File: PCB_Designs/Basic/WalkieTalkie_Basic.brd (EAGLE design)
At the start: 27.9 x 27.9 mm, 35 parts, among them Q1 MOSFET-NCHANNELBSS123LT1G, U1 ATMEGA328P

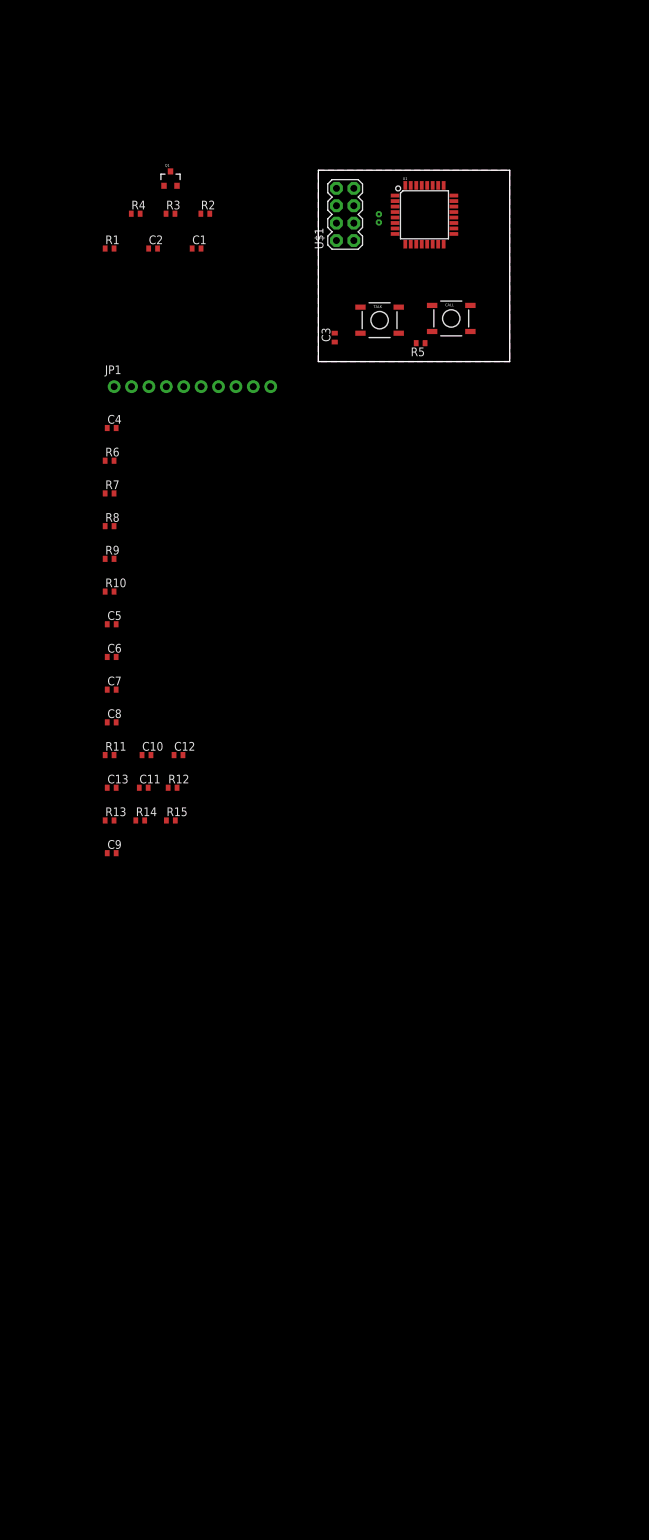
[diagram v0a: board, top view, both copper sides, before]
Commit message: updating pcb design with labels, removed extra button, added library part for nRF24L01 breakout, etc
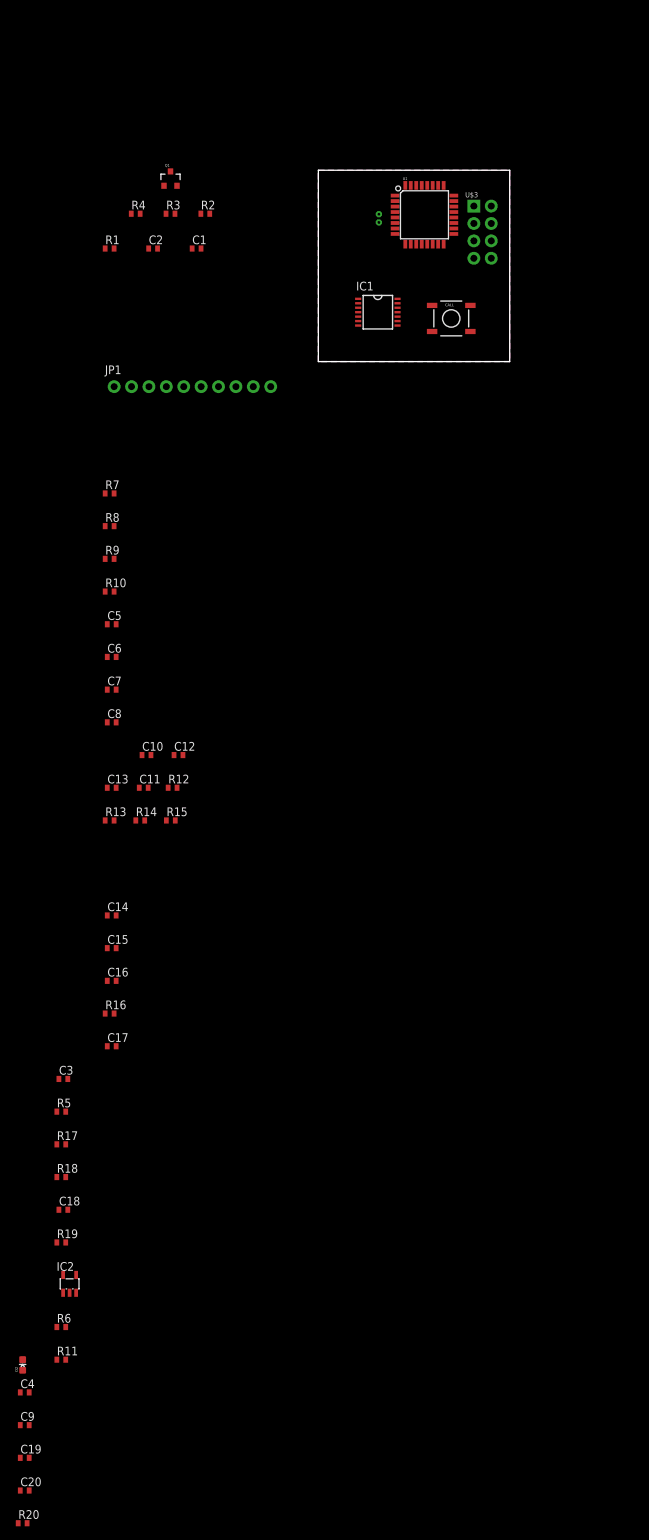
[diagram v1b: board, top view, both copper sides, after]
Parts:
- removed TALK: TAC_SWITCHSMD, SparkFun-Retired:TACTILE-SWITCH-SMD
- removed U$1: M04X2, SparkFun-Connectors:2X4
- added C14, C15, C16, C17, C19, C20: 100n, resistor:C0402
- added C18: 10n, resistor:C0402
- added D2: RED, SparkFun-LED:LED-0603
- added IC1: AD8609RU, analog-devices:TSSOP14
- added IC2: AD8603UJ, analog-devices:SOT23-5
- added R16: 10k, resistor:R0402
- added R17, R18, R19: 1.5k, resistor:R0402
- added R20: 1k, resistor:R0402
- added U$3: NRF24L01-BREAKOUT, Orlando:NRF24L01-BREAKOUT
- C3: value 100n -> 10n
- C4, C9: value 10n -> 100n
- R11, R6: value 1.5M -> 1.5k
- R5: value 10k -> 1.5M
- moved C4 141.4 mm to (-42.9, -150.5)
- moved R6 126.7 mm to (-37.5, -141.0)
- moved R5 123.9 mm to (-37.5, -109.5), turned to 0 degrees
- moved C3 115.3 mm to (-37.2, -104.7), turned to 0 degrees
- moved R11 88.6 mm to (-37.5, -145.7)
- moved C9 84.5 mm to (-42.9, -155.3)
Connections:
- net N$1 renamed D13-SCK
- net N$2 renamed D12-MISO
- net N$3 renamed D11-MOSI
- net N$4 renamed D10
- removed net N$15: C9.2, R11.2, R12.2
- new net 1/2-VDD: IC1.12, IC1.5, IC2.1, IC2.4
- new net A0-MIC: Q1.3, R1.2, R2.1, U1.23
- new net CE: U$3.3
- new net CSN: U$3.4
- new net D2: U1.32
- new net D3: U1.1
- new net D4: U1.2
- new net D5: U1.9
- new net D6: U1.10
- new net D7: U1.11
- new net D8: U1.12
- new net D9: U1.13
- new net DTR: C17.2
- new net IRQ: U$3.8
- new net MISO: U$3.7
- new net MOSI: U$3.6
- new net N$20: C14.2, U$2.2, U1.7
- new net N$21: C15.2, U$2.1, U1.8
- new net N$22: C16.2, U1.20
- new net N$23: C3.2, R17.2
- new net N$24: IC1.6, R17.1, R18.2
- new net N$25: IC1.7, R18.1
- new net N$26: C18.1, IC1.8, IC1.9
- new net N$27: IC1.13, R19.1, R5.2
- new net N$28: C18.2, R19.2
- new net N$29: IC1.14, R5.1
- new net N$37: JP1.10
- new net N$38: JP1.9
- new net N$39: JP1.8
- new net N$40: JP1.7
- new net N$41: JP1.6
- new net N$42: JP1.5
- new net N$43: JP1.4
- new net N$44: JP1.3
- new net N$45: JP1.2
- new net N$46: JP1.1
- new net RESET: C17.1, R16.1, U1.29
- new net RXI: U1.30
- new net SCK: U$3.5
- new net TXO: U1.31
- net 3.3V: now also C19.1, C20.1, C4.1, C9.1, IC1.4, IC2.5, R16.2, R6.1, U$3.2, U1.18, U1.4, U1.6; no longer C3.2, TALK.1
- net BUTTON: no longer TALK.4
- net GND: now also C14.1, C15.1, C16.1, C19.2, C20.2, C4.2, C9.2, IC1.11, IC2.2, R11.2, R20.1, U$3.1, U1.21, U1.3, U1.5; no longer R11.1, R5.1, R6.1
- net N$13: now also IC1.3
- net N$18: now also IC1.10
- net N$6: now also D2.C, R20.2; no longer Q1.3, R1.2, R2.1
- net N$7: now also IC1.1, IC1.2; no longer R5.2, TALK.2
- net N$9: now also IC2.3, R11.1; no longer C4.2, R7.2
- net SP1: now also R7.2; no longer C4.1
- net SP2: now also R12.2; no longer C9.1

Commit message: updating PCB design with buttons, LED indicators, etc.
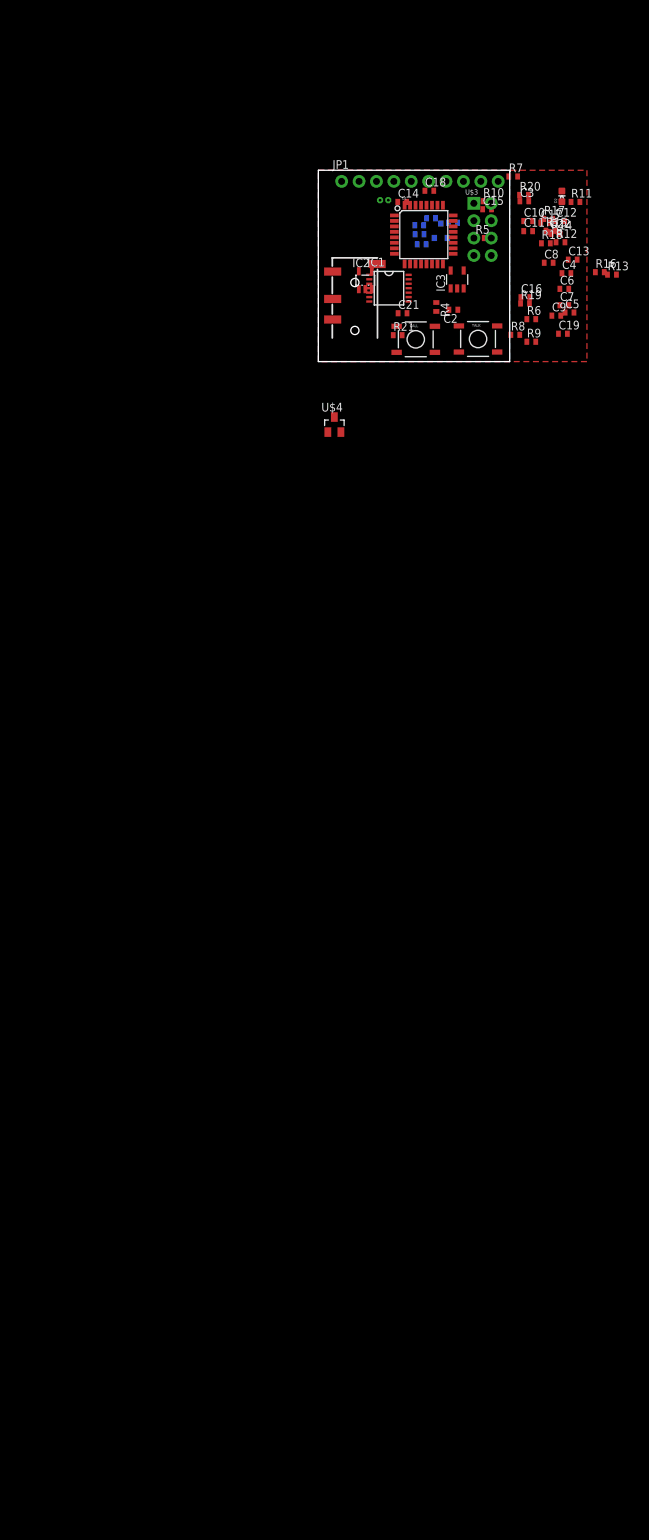
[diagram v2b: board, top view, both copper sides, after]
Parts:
- added C21, C22: 100n, resistor:C0402
- added IC3: MCP601OT, linear:SOT23-5
- added R21: 10k, resistor:R0402
- added TALK: TAC_SWITCHSMD, SparkFun-Retired:TACTILE-SWITCH-SMD
- added U$1: AUDIO-JACK3, SparkFun-Connectors:AUDIO-JACK-TRRS-SMD
- added U$4: AP2120N, OrlandoRonMod:SOT23
- moved R20 207.3 mm to (30.0, 24.3)
- moved C20 195.4 mm to (19.7, 20.3), flipped to the bottom
- moved D2 187.9 mm to (35.6, 24.0)
- moved R11 185.0 mm to (37.5, 23.3)
- moved C19 182.0 mm to (35.7, 4.06)
- moved C4 181.6 mm to (36.2, 12.9)
- moved C9 179.6 mm to (34.7, 6.71)
- moved R6 162.4 mm to (31.1, 6.20)
- moved C18 158.1 mm to (16.2, 24.9)
- moved R18 153.6 mm to (33.2, 17.3)
- moved R19 152.9 mm to (30.2, 8.48)
- moved IC2 152.8 mm to (6.86, 11.9)
- moved R17 152.7 mm to (33.6, 20.8)
- moved C3 144.8 mm to (30.1, 23.4)
- moved R5 141.4 mm to (23.6, 18.0)
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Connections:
- removed net BUTTON: CALL.4
- removed net N$25: IC1.7, R18.1
- removed net N$29: IC1.14, R5.1
- new net N$1: C21.2, CALL.1, R21.2
- new net N$15: U$1.EARTH
- new net N$2: C2.2, R4.2, TALK.1
- new net N$3: IC1.7, R18.1, U$1.RING1
- new net N$4: IC1.14, R5.1, U$1.TIP
- new net TALK/CALL: CALL.4, TALK.4, U1.24
- net 3.3V: now also C22.1, IC3.2, R21.1, R4.1; no longer C2.2, CALL.1
- net D3: now also IC3.1, IC3.4
- net D6: now also D2.A, IC3.3
- net GND: now also C2.1, C21.1, C22.2, CALL.2, IC3.5, TALK.2; no longer R4.1
- net N$12: now also U$1.RING2; no longer C2.1, CALL.2, R4.2

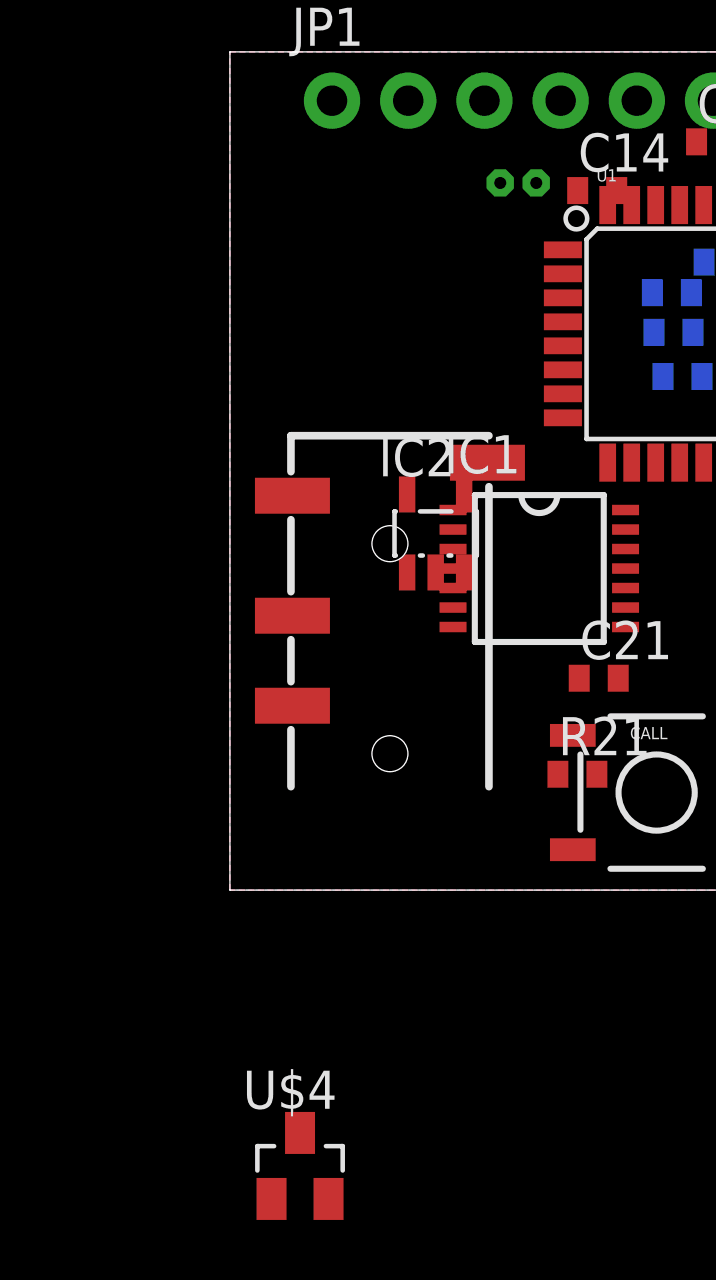
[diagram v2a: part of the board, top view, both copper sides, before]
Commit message: updating PCB design and adding more datasheets
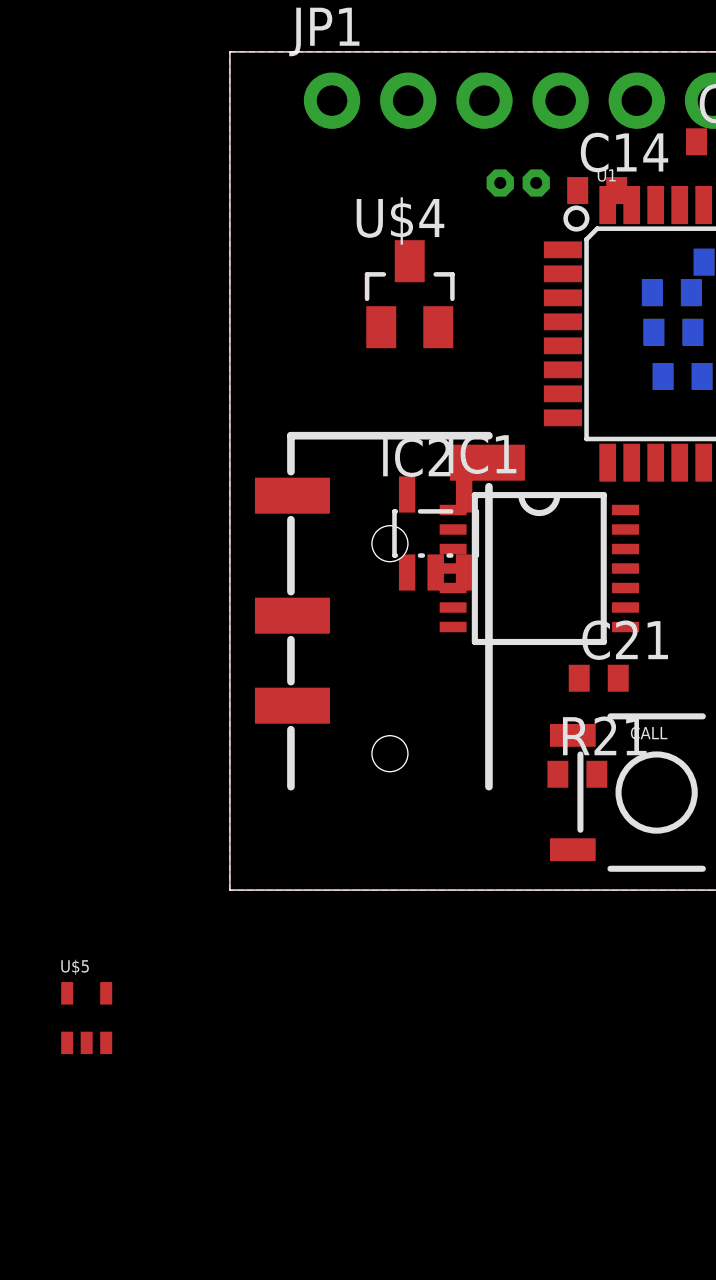
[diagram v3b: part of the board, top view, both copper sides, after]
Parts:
- added U$5: MIC5365/6, Orlando:SC-70-5
- moved U$4 29.3 mm to (5.99, 19.9)
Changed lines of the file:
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@@
 <element name="C21" library="resistor" package="C0402" value="100n" x="12.2936" y="7.0612"/>
 <element name="U$1" library="SparkFun-Connectors" package="AUDIO-JACK-TRRS-SMD" value="AUDIO-JACK3" x="5.334" y="2.9464" rot="R90"/>
-<element name="U$4" library="OrlandoRonMod" package="SOT23" value="AP2120N" x="2.3368" y="-9.1948"/>
+<element name="U$4" library="OrlandoRonMod" package="SOT23" value="AP2120N" x="5.9944" y="19.8628"/>
+<element name="U$5" library="Orlando" package="SC-70-5" value="MIC5365/6" x="-4.7752" y="-4.2672"/>
 </elements>
 <signals>

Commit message: more PCB updates and more datasheets
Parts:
- removed C16: 100n, resistor:C0402
- removed JP1: M10NO_SILK_PTH_FEMALE, SparkFun-Connectors:1X10_NO_SILK
- removed U$5: MIC5365/6, Orlando:SC-70-5
- removed U1: ATMEGA328P, SparkFun-DigitalIC:TQFP32-08
- added ARDUINO: ATMEGA328P, SparkFun-DigitalIC:TQFP32-08
- added C23, C24: 100n, resistor:C0402
- added LDO: MIC5365/6, Orlando:SC-70-5
- added MIC: MIC_CMC-5042PF-AC, Orlando:MIC_01
- added PROGRAM/BOOTLOAD: M10NO_SILK_PTH_FEMALE, SparkFun-Connectors:1X10_NO_SILK
- added XTAL: CRYSTAL-CA-310, OrlandoRonMod:CA-301
- U$2: value CRYSTAL-CA-310 -> PS1240P02CT3P; device OrlandoRonMod:CA-301 -> Orlando:PIEZO-1
- U$4: value AP2120N -> BATT-CONNECT; device OrlandoRonMod:SOT23 -> OrlandoRonMod:HOLE
- moved R13 45.0 mm to (3.20, 33.9)
- moved C6 41.4 mm to (3.45, 36.3)
- moved C7 40.7 mm to (5.49, 35.3)
- moved C5 39.5 mm to (3.86, 29.2)
- moved C13 36.3 mm to (4.88, 31.4), turned to 90 degrees
- moved R11 33.1 mm to (4.42, 24.4), flipped to the bottom, turned to 90 degrees
- moved R17 32.5 mm to (1.98, 28.5)
- moved C11 31.3 mm to (1.83, 31.2), turned to 90 degrees
- moved U$4 30.2 mm to (29.5, 38.9)
- moved R14 29.5 mm to (7.16, 29.4)
- moved C10 29.3 mm to (3.51, 31.6), turned to 90 degrees
- moved IC1 24.4 mm to (4.78, 34.5)
- moved C22 22.5 mm to (12.1, 21.9), flipped to the bottom, turned to 270 degrees
- moved R7 21.9 mm to (37.6, 7.11)
- moved C4 21.4 mm to (28.1, 32.7), turned to 90 degrees
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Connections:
- removed net CE: U$3.3
- removed net CSN: U$3.4
- removed net D10: U1.14
- removed net D2: U1.32
- removed net D7: U1.11
- removed net D8: U1.12
- removed net D9: U1.13
- removed net IRQ: U$3.8
- removed net MISO: U$3.7
- removed net MOSI: U$3.6
- removed net N$22: C16.2, U1.20
- removed net N$37: JP1.10
- removed net N$38: JP1.9
- removed net N$39: JP1.8
- removed net N$40: JP1.7
- removed net N$41: JP1.6
- removed net N$42: JP1.5
- removed net N$43: JP1.4
- removed net N$44: JP1.3
- removed net N$45: JP1.2
- removed net N$46: JP1.1
- removed net SCK: U$3.5
- removed net SP1: R7.2
- removed net SP2: R12.2
- new net D10-SPEAK2: ARDUINO.14, R12.2
- new net D2-IRQ: ARDUINO.32, U$3.8
- new net D7-CE: ARDUINO.11, U$3.3
- new net D8-CSN: ARDUINO.12, U$3.4
- new net D9-SPEAK1: ARDUINO.13, R7.2
- new net V_BATT: C23.1, LDO.1, LDO.3, U$4.P$2
- net 3.3V: now also ARDUINO.18, ARDUINO.4, ARDUINO.6, C24.1, LDO.5, PROGRAM/BOOTLOAD.8; no longer U1.18, U1.4, U1.6
- net A0-MIC: now also ARDUINO.23; no longer U1.23
- net D11-MOSI: now also ARDUINO.15, PROGRAM/BOOTLOAD.3, U$3.6; no longer U1.15
- net D12-MISO: now also ARDUINO.16, PROGRAM/BOOTLOAD.2, U$3.7; no longer U1.16
- net D13-SCK: now also ARDUINO.17, PROGRAM/BOOTLOAD.1, U$3.5; no longer U1.17
- net D3: now also ARDUINO.1, U$2.+; no longer U1.1
- net D4: now also ARDUINO.2; no longer U1.2
- net D5: now also ARDUINO.9; no longer U1.9
- net D6: now also ARDUINO.10, R20.2; no longer D2.A, U1.10
- net DTR: now also PROGRAM/BOOTLOAD.5
- net GND: now also ARDUINO.21, ARDUINO.3, ARDUINO.5, C23.2, C24.2, D2.C, LDO.2, MIC.-, PROGRAM/BOOTLOAD.10, PROGRAM/BOOTLOAD.9, U$2.-, U$4.P$1; no longer C16.1, R20.1, U1.21, U1.3, U1.5
- net N$20: now also ARDUINO.7, XTAL.2; no longer U$2.2, U1.7
- net N$21: now also ARDUINO.8, XTAL.1; no longer U$2.1, U1.8
- net N$6: now also D2.A, R20.1; no longer D2.C, R20.2
- net N$8: now also MIC.+
- net RESET: now also ARDUINO.29, PROGRAM/BOOTLOAD.4; no longer U1.29
- net RXI: now also ARDUINO.30, PROGRAM/BOOTLOAD.7; no longer U1.30
- net TALK/CALL: now also ARDUINO.24; no longer U1.24
- net TXO: now also ARDUINO.31, PROGRAM/BOOTLOAD.6; no longer U1.31
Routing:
- net D12-MISO: track 0.00 -> 27.3 mm, vias 0 -> 1
- net D2-IRQ: track 0.00 -> 25.2 mm
- net TALK/CALL: track 0.00 -> 25.1 mm, vias 0 -> 2
- net D11-MOSI: track 0.00 -> 22.4 mm, vias 0 -> 1
- net D13-SCK: track 0.00 -> 21.8 mm, vias 0 -> 1
- net D3: track 0.00 -> 16.7 mm
- net D8-CSN: track 0.00 -> 14.7 mm
- net D6: track 0.00 -> 14.4 mm, vias 0 -> 2
- net RESET: track 0.00 -> 14.0 mm, vias 0 -> 1
- net D7-CE: track 0.00 -> 9.58 mm, vias 0 -> 2
- net N$20: track 0.00 -> 6.82 mm
- net N$21: track 0.00 -> 5.64 mm
- net N$1: track 0.00 -> 4.11 mm, vias 0 -> 1
- net N$6: track 0.00 -> 2.03 mm
- removed copper zone on layer 1, net 3.3V
- removed copper zone on layer 16, net GND
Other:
- board size 27.9 x 27.9 mm -> 33 x 50.8 mm

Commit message: more updates
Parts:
- moved C4 9.61 mm to (37.7, 33.2)
- moved LDO 8.95 mm to (38.0, 39.4)
- moved C24 7.18 mm to (36.9, 36.4)
- moved C23 6.80 mm to (35.6, 34.2)
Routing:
- net D12-MISO: track 27.3 -> 19.8 mm, vias 1 -> 0
- net D13-SCK: track 21.8 -> 15.7 mm
- net D7-CE: track 9.58 -> 14.3 mm, vias 2 -> 1
- net D2-IRQ: track 25.2 -> 29.8 mm, vias 0 -> 2
- net D11-MOSI: track 22.4 -> 26.5 mm, vias 1 -> 2
- net D8-CSN: track 14.7 -> 12.8 mm, vias 0 -> 1
- added copper zone on layer 1, net 3.3V
- added copper zone on layer 16, net GND

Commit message: updates to PCB
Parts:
- C14, C15: value 100n -> 22p
- moved C3 39.2 mm to (2.84, 28.2), flipped to the bottom, turned to 270 degrees
- moved R5 39.1 mm to (2.69, 28.9)
- moved R7 39.0 mm to (11.6, 36.2), flipped to the bottom, turned to 90 degrees
- moved C8 39.0 mm to (3.76, 36.2), flipped to the bottom, turned to 270 degrees
- moved C9 37.5 mm to (8.18, 33.1), turned to 90 degrees
- moved C19 34.2 mm to (11.8, 28.5), flipped to the bottom, turned to 270 degrees
- moved C12 33.2 mm to (6.35, 33.3), flipped to the bottom, turned to 90 degrees
- moved R9 32.0 mm to (7.11, 36.2), flipped to the bottom, turned to 90 degrees
- moved R15 31.9 mm to (5.23, 33.3), flipped to the bottom, turned to 270 degrees
- moved R16 30.8 mm to (15.9, 30.8), flipped to the bottom, turned to 180 degrees
- moved R19 30.8 mm to (1.63, 31.6), turned to 90 degrees
- moved R18 30.2 mm to (8.33, 30.3), turned to 270 degrees
- moved R12 29.5 mm to (11.9, 33.3), flipped to the bottom, turned to 90 degrees
- moved R8 27.9 mm to (9.35, 36.2), flipped to the bottom, turned to 270 degrees
- moved C17 23.9 mm to (15.2, 36.1), flipped to the bottom, turned to 90 degrees
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- renumbered U$4 to LIPO
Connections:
- net 1/2-VDD: now also IC1.10; no longer IC1.5
- net D10-SPEAK2: now also R7.2; no longer R12.2
- net D9-SPEAK1: now also R12.2; no longer R7.2
- net N$18: now also IC1.5; no longer IC1.10
- net N$24: now also IC1.13; no longer IC1.6
- net N$26: now also IC1.6, IC1.7; no longer IC1.8, IC1.9
- net N$27: now also IC1.9; no longer IC1.13
- net N$3: now also IC1.14; no longer IC1.7
- net N$4: now also IC1.8; no longer IC1.14
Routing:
- net N$3: track 0.00 -> 18.4 mm
- net TXO: track 0.00 -> 12.8 mm, vias 0 -> 1
- net D10-SPEAK2: track 0.00 -> 11.9 mm, vias 0 -> 1
- net 1/2-VDD: track 0.00 -> 11.7 mm, vias 0 -> 1
- net RXI: track 0.00 -> 10.1 mm
- net N$7: track 0.00 -> 9.69 mm, vias 0 -> 1
- net D9-SPEAK1: track 0.00 -> 9.32 mm, vias 0 -> 1
- net N$13: track 0.00 -> 7.24 mm, vias 0 -> 1
- net N$24: track 0.00 -> 7.21 mm, vias 0 -> 1
- net N$4: track 0.00 -> 4.94 mm
- net N$18: track 0.00 -> 4.70 mm, vias 0 -> 1
- net N$27: track 0.00 -> 4.11 mm
- net N$9: track 0.00 -> 3.34 mm
- net GND: track 0.00 -> 2.76 mm, vias 0 -> 1
- net N$23: track 0.00 -> 2.64 mm
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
